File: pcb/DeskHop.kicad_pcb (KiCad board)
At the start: 2 copper layers, 66.9 x 74.5 mm, 12 parts, among them J1 Keyboard In, J2 Debug2, J3 Debug1, J4 Mouse In, U1 Pico Primary, U2 Pico Secondary, U4 ADuM1201BR

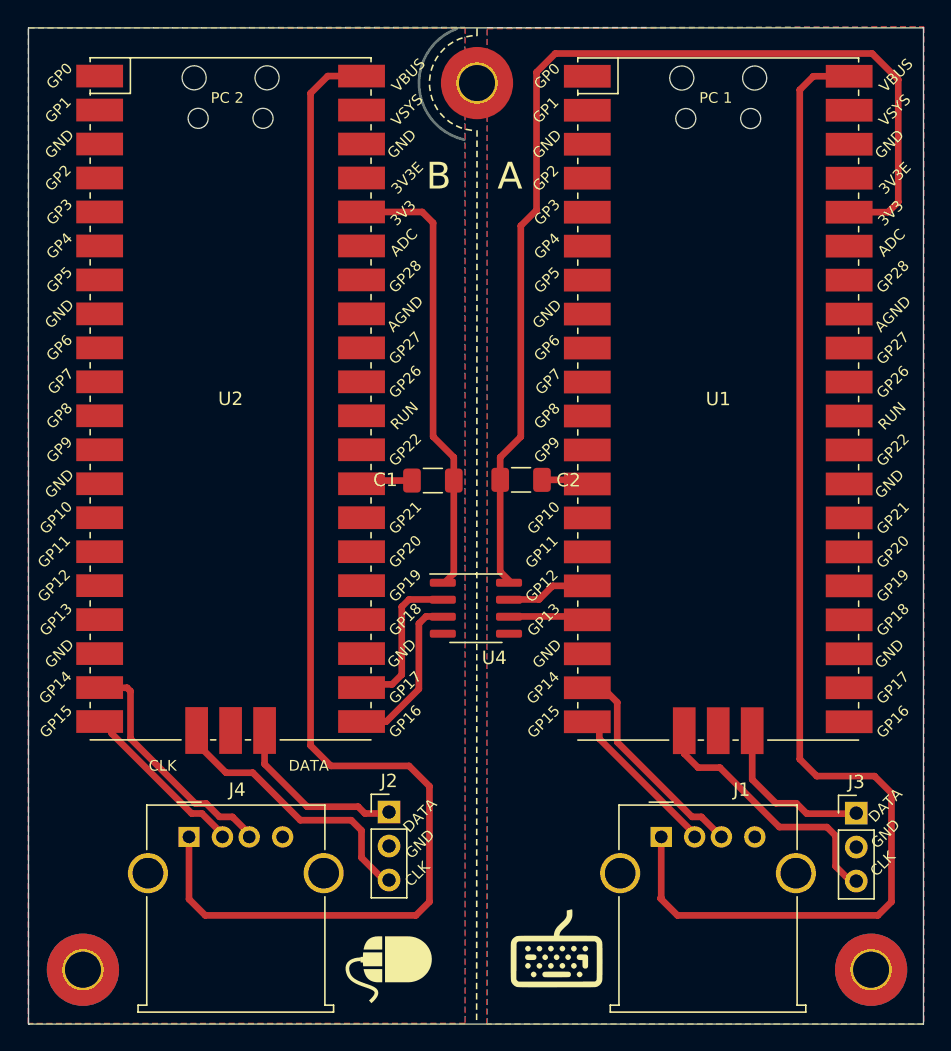
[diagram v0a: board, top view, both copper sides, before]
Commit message: Cleanup, Refactoring, Silkscreen update
- Code refactor, still far from great but a bit less crappy
- Unify behavior - Mouse Zoom feature was made toggle and
  moved from ALT to Right ALT + Right CTRL to avoid interfering
  with OS
- Added optional screensaver "Pong" mode, prevents sleep and it's fun
- Updated README
- Added more visible pin1 marking on PCB for digital isolator
- Marked pins to solder with a star *
- Added checksum and version format support for flash config
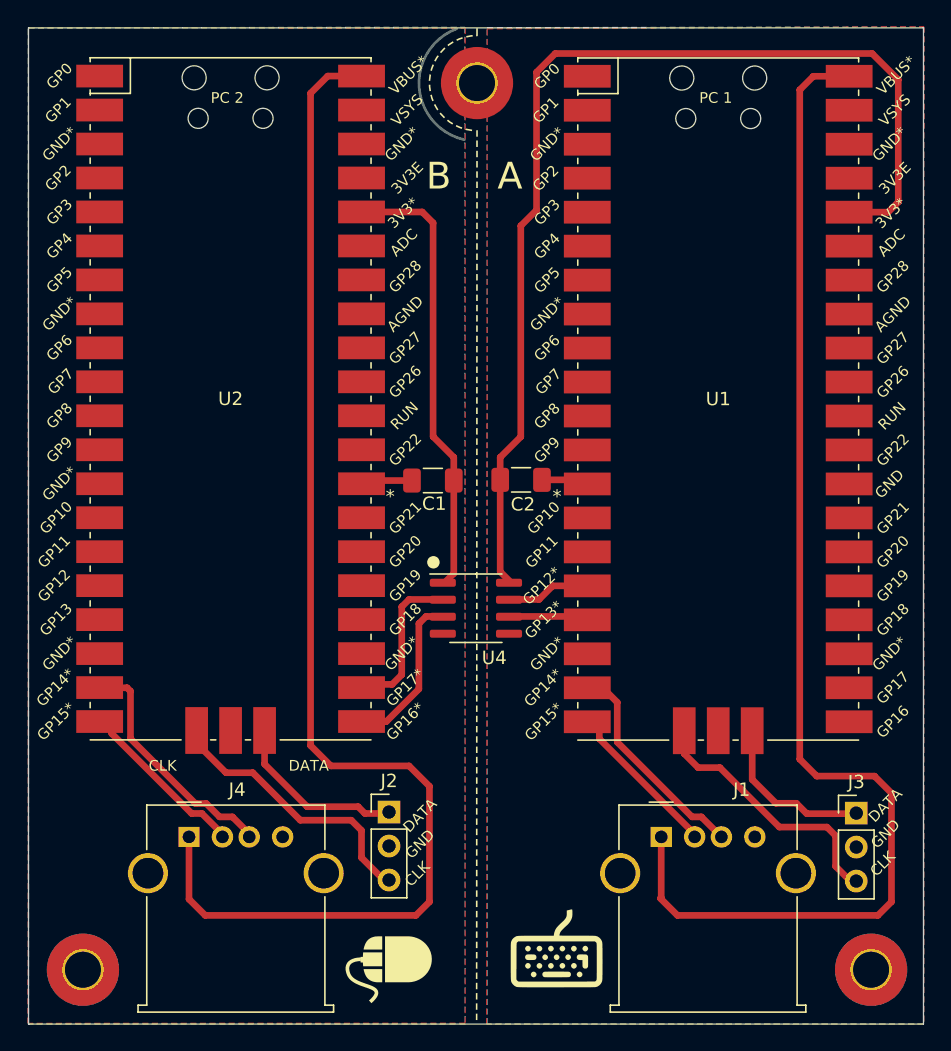
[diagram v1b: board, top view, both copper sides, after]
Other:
- board text added: "*"
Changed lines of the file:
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@@
         (effects (font (size 0.8 0.8) (thickness 0.15)))
     )
-    (fp_text user "GP12" (at -13.2 13.97 45) (layer "F.SilkS")
+    (fp_text user " GP12*" (at -13.2 13.97 45) (layer "F.SilkS")
         (effects (font (size 0.8 0.8) (thickness 0.15)))
     )
-    (fp_text user "GND" (at -12.8 19.05 45) (layer "F.SilkS")
+    (fp_text user " GND*" (at -12.8 19.05 45) (layer "F.SilkS")
         (effects (font (size 0.8 0.8) (thickness 0.15)))
     )
@@
         (effects (font (size 0.8 0.8) (thickness 0.15)))
     )
-    (fp_text user "GP15" (at -13.054 24.13 45) (layer "F.SilkS")
+    (fp_text user " GP15*" (at -13.054 24.13 45) (layer "F.SilkS")
         (effects (font (size 0.8 0.8) (thickness 0.15)))
     )
-    (fp_text user "GND" (at 12.8 19.05 45) (layer "F.SilkS")
+    (fp_text user " GND*" (at 12.8 19.05 45) (layer "F.SilkS")
         (effects (font (size 0.8 0.8) (thickness 0.15)))
     )
-    (fp_text user "GND" (at -12.8 -6.35 45) (layer "F.SilkS")
+    (fp_text user " GND*" (at -12.8 -6.35 45) (layer "F.SilkS")
         (effects (font (size 0.8 0.8) (thickness 0.15)))
     )
-    (fp_text user "GP13" (at -13.054 16.51 45) (layer "F.SilkS")
+    (fp_text user " GP13*" (at -13.054 16.51 45) (layer "F.SilkS")
         (effects (font (size 0.8 0.8) (thickness 0.15)))
     )
@@
         (effects (font (size 0.8 0.8) (thickness 0.15)))
     )
-    (fp_text user "VBUS" (at 13.3 -24.2 45) (layer "F.SilkS")
+    (fp_text user " VBUS*" (at 13.3 -24.2 45) (layer "F.SilkS")
         (effects (font (size 0.8 0.8) (thickness 0.15)))
     )
-    (fp_text user "GND" (at -12.8 -19.05 45) (layer "F.SilkS")
+    (fp_text user " GND*" (at -12.8 -19.05 45) (layer "F.SilkS")
         (effects (font (size 0.8 0.8) (thickness 0.15)))
     )
@@
         (effects (font (size 0.8 0.8) (thickness 0.15)))
     )
-    (fp_text user "3V3" (at 12.9 -13.9 45) (layer "F.SilkS")
+    (fp_text user " 3V3*" (at 12.9 -13.9 45) (layer "F.SilkS")
         (effects (font (size 0.8 0.8) (thickness 0.15)))
     )
-    (fp_text user "GND" (at 12.8 -19.05 45) (layer "F.SilkS")
+    (fp_text user " GND*" (at 12.8 -19.05 45) (layer "F.SilkS")
         (effects (font (size 0.8 0.8) (thickness 0.15)))
     )
@@
         (effects (font (size 0.8 0.8) (thickness 0.15)))
     )
-    (fp_text user "GP14" (at -13.1 21.59 45) (layer "F.SilkS")
+    (fp_text user " GP14*" (at -13.1 21.59 45) (layer "F.SilkS")
         (effects (font (size 0.8 0.8) (thickness 0.15)))
     )
@@
         (effects (font (size 0.8 0.8) (thickness 0.15)))
     )
-    (fp_text user "GND" (at 12.8 -19.05 45) (layer "F.SilkS")
+    (fp_text user " GND*" (at 12.8 -19.05 45) (layer "F.SilkS")
         (effects (font (size 0.8 0.8) (thickness 0.15)))
     )
@@
         (effects (font (size 0.8 0.8) (thickness 0.15)))
     )
-    (fp_text user "GP15" (at -13.054 24.13 45) (layer "F.SilkS")
+    (fp_text user " GP15*" (at -13.054 24.13 45) (layer "F.SilkS")
         (effects (font (size 0.8 0.8) (thickness 0.15)))
     )
@@
         (effects (font (size 0.8 0.8) (thickness 0.15)))
     )
-    (fp_text user "VBUS" (at 13.3 -24.2 45) (layer "F.SilkS")
+    (fp_text user " VBUS*" (at 13.3 -24.2 45) (layer "F.SilkS")
         (effects (font (size 0.8 0.8) (thickness 0.15)))
     )
@@
         (effects (font (size 0.8 0.8) (thickness 0.15)))
     )
-    (fp_text user "GND" (at -12.8 19.05 45) (layer "F.SilkS")
+    (fp_text user " GND*" (at -12.8 19.05 45) (layer "F.SilkS")
         (effects (font (size 0.8 0.8) (thickness 0.15)))
     )
@@
         (effects (font (size 0.8 0.8) (thickness 0.15)))
     )
-    (fp_text user "GND" (at -12.8 -19.05 45) (layer "F.SilkS")
+    (fp_text user " GND*" (at -12.8 -19.05 45) (layer "F.SilkS")
         (effects (font (size 0.8 0.8) (thickness 0.15)))
     )
-    (fp_text user "GP17" (at 13.054 21.59 45) (layer "F.SilkS")
+    (fp_text user " GP17*" (at 13.054 21.59 45) (layer "F.SilkS")
         (effects (font (size 0.8 0.8) (thickness 0.15)))
     )
@@
         (effects (font (size 0.8 0.8) (thickness 0.15)))
     )
-    (fp_text user "GND" (at -12.8 6.35 45) (layer "F.SilkS")
+    (fp_text user " GND*" (at -12.8 6.35 45) (layer "F.SilkS")
         (effects (font (size 0.8 0.8) (thickness 0.15)))
     )
@@
         (effects (font (size 0.8 0.8) (thickness 0.15)))
     )
-    (fp_text user "GP14" (at -13.1 21.59 45) (layer "F.SilkS")
+    (fp_text user " GP14*" (at -13.1 21.59 45) (layer "F.SilkS")
         (effects (font (size 0.8 0.8) (thickness 0.15)))
     )
@@
         (effects (font (size 0.8 0.8) (thickness 0.15)))
     )
-    (fp_text user "3V3" (at 12.9 -13.9 45) (layer "F.SilkS")
+    (fp_text user " 3V3*" (at 12.9 -13.9 45) (layer "F.SilkS")
         (effects (font (size 0.8 0.8) (thickness 0.15)))
     )
-    (fp_text user "GP16" (at 13.054 24.13 45) (layer "F.SilkS")
+    (fp_text user " GP16*" (at 13.054 24.13 45) (layer "F.SilkS")
         (effects (font (size 0.8 0.8) (thickness 0.15)))
     )
-    (fp_text user "GND" (at -12.8 -6.35 45) (layer "F.SilkS")
+    (fp_text user " GND*" (at -12.8 -6.35 45) (layer "F.SilkS")
         (effects (font (size 0.8 0.8) (thickness 0.15)))
     )
@@
         (effects (font (size 0.8 0.8) (thickness 0.15)))
     )
-    (fp_text user "GND" (at 12.8 19.05 45) (layer "F.SilkS")
+    (fp_text user " GND*" (at 12.8 19.05 45) (layer "F.SilkS")
         (effects (font (size 0.8 0.8) (thickness 0.15)))
     )
@@
     (property "ki_keywords" "cap capacitor")
     (attr smd)
-    (fp_text reference "C2" (at 3.5429 0.0254) (layer "F.SilkS")
+    (fp_text reference "C2" (at 0.134809 1.830335) (layer "F.SilkS")
         (effects (font (size 1 1) (thickness 0.15)))
     )
@@
     (property "ki_keywords" "cap capacitor")
     (attr smd)
-    (fp_text reference "C1" (at 3.556 0.0508) (layer "F.SilkS")
+    (fp_text reference "C1" (at -0.099564 -1.727201) (layer "F.SilkS")
         (effects (font (size 1 1) (thickness 0.15)))
     )
@@
     )
     (stroke (width 0) (type solid)) (fill solid) (layer "F.SilkS"))
+  (gr_circle (center 64.048728 81.041328) (end 64.455128 81.041328)
+    (stroke (width 0.12) (type solid)) (fill solid) (layer "F.SilkS"))
   (gr_poly
     (pts
@@
     (effects (font (size 1.1 1.1) (thickness 0.15)) (justify left bottom mirror))
   )
+  (gr_text "*" (at 60.4774 76.708) (layer "F.SilkS")
+    (effects (font (size 1 1) (thickness 0.15)) (justify left bottom))
+  )
   (gr_text "PC 1" (at 83.9216 46.7868) (layer "F.SilkS")
     (effects (font (size 0.8 0.8) (thickness 0.15)) (justify left bottom))
@@
     (effects (font (size 0.8 0.8) (thickness 0.15)))
   )
+  (gr_text "*" (at 72.9488 76.708) (layer "F.SilkS")
+    (effects (font (size 1 1) (thickness 0.15)) (justify left bottom))
+  )
   (gr_text "A" (at 68.834 53.34) (layer "F.SilkS")
